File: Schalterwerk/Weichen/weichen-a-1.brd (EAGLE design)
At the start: 86 x 30.5 mm, 44 parts, among them J1 PHNX_2P_508CONN_1017491, Q1 P-MOSFET, Q2 P-MOSFET, Q3 P-MOSFET, Q4 P-MOSFET, X1 PHNX_4P_508CONN_1017493, X2 PHNX_4P_350CONN_1984989_PXC, X3 PHNX_4P_350CONN_1984989_PXC, X4 RJ45-JACK

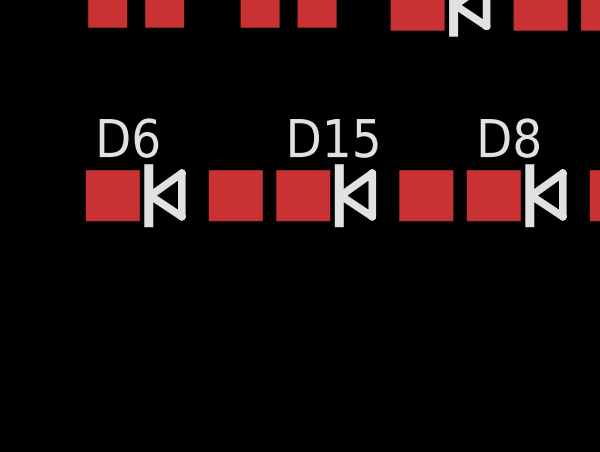
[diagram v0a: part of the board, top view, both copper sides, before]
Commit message: Closes out first release of Weichenschaltung.
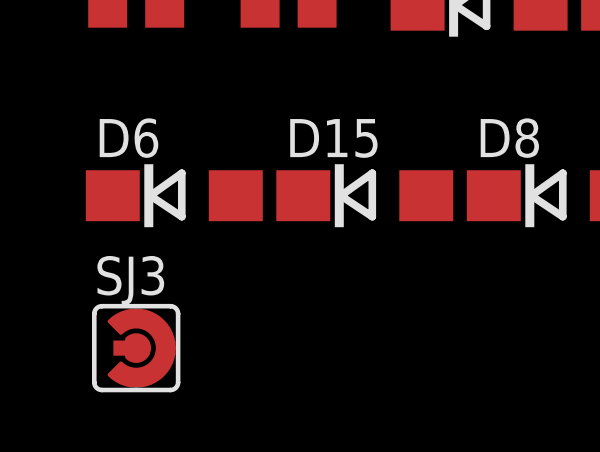
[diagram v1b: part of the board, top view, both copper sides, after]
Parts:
- added SJ3: (no value), eagleparts:SJ_RND2
- R1, R2, R3, R4: value 5k -> 10k
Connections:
- net GND: now also SJ3.P$1
- net L2: now also D10.C, D12.C, D3.A, D6.C, D8.C, R10.2, X1.5, X1.6; no longer D10.A, D11.A, D9.A, X1.3, X1.4
- net L3: now also D10.A, D11.A, D9.A, SJ3.P$2, X1.3, X1.4; no longer D10.C, D12.C, D3.A, D6.C, D8.C, R10.2, X1.5, X1.6
- net N$16: now also OK1.2, OK1.4; no longer OK1.6, OK1.8
- net N$24: now also OK1.1; no longer OK1.5
- net N$25: now also OK1.3; no longer OK1.7
- net N$27: now also OK1.16; no longer OK1.12
- net N$30: now also OK1.14; no longer OK1.10
- net N$35: now also OK1.15; no longer OK1.11
- net N$37: now also OK1.13; no longer OK1.9
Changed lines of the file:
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@@
 <attribute name="VALUE" x="4.35" y="-419.04" size="1.27" layer="27" align="top-left"/>
 </element>
-<element name="R1" library="rcl" library_urn="urn:adsk.eagle:library:334" package="R0805" package3d_urn="urn:adsk.eagle:package:23553/2" value="5k" x="2.54" y="-424.18" smashed="yes">
+<element name="R1" library="rcl" library_urn="urn:adsk.eagle:library:334" package="R0805" package3d_urn="urn:adsk.eagle:package:23553/2" value="10k" x="2.54" y="-424.18" smashed="yes">
 <attribute name="NAME" x="1.905" y="-422.91" size="1.27" layer="25"/>
 <attribute name="POPULARITY" value="86" x="2.54" y="-424.18" size="1.778" layer="27" display="off"/>
@@
 <attribute name="VALUE" x="4.35" y="-443.17" size="1.27" layer="27" align="top-left"/>
 </element>
-<element name="R2" library="rcl" library_urn="urn:adsk.eagle:library:334" package="R0805" package3d_urn="urn:adsk.eagle:package:23553/2" value="5k" x="2.54" y="-448.31" smashed="yes">
+<element name="R2" library="rcl" library_urn="urn:adsk.eagle:library:334" package="R0805" package3d_urn="urn:adsk.eagle:package:23553/2" value="10k" x="2.54" y="-448.31" smashed="yes">
 <attribute name="NAME" x="1.905" y="-447.04" size="1.27" layer="25"/>
 <attribute name="POPULARITY" value="86" x="2.54" y="-448.31" size="1.778" layer="27" display="off"/>
@@
 <attribute name="VALUE" x="4.35" y="-573.98" size="1.27" layer="27" align="top-left"/>
 </element>
-<element name="R3" library="rcl" library_urn="urn:adsk.eagle:library:334" package="R0805" package3d_urn="urn:adsk.eagle:package:23553/2" value="5k" x="7.62" y="-590.55" smashed="yes">
+<element name="R3" library="rcl" library_urn="urn:adsk.eagle:library:334" package="R0805" package3d_urn="urn:adsk.eagle:package:23553/2" value="10k" x="7.62" y="-590.55" smashed="yes">
 <attribute name="NAME" x="6.985" y="-589.28" size="1.27" layer="25"/>
 <attribute name="POPULARITY" value="86" x="2.54" y="-579.12" size="1.778" layer="27" display="off"/>
@@
 <attribute name="VALUE" x="4.35" y="-585.41" size="1.27" layer="27" align="top-left"/>
 </element>
-<element name="R4" library="rcl" library_urn="urn:adsk.eagle:library:334" package="R0805" package3d_urn="urn:adsk.eagle:package:23553/2" value="5k" x="2.54" y="-590.55" smashed="yes">
+<element name="R4" library="rcl" library_urn="urn:adsk.eagle:library:334" package="R0805" package3d_urn="urn:adsk.eagle:package:23553/2" value="10k" x="2.54" y="-590.55" smashed="yes">
 <attribute name="NAME" x="1.905" y="-589.28" size="1.27" layer="25"/>
 <attribute name="POPULARITY" value="86" x="2.54" y="-603.25" size="1.778" layer="27" display="off"/>
@@
 <attribute name="POPULARITY" value="14" x="3.81" y="-641.35" size="1.778" layer="27" display="off"/>
 <attribute name="VALUE" x="20.22" y="-599.456" size="1.27" layer="27" ratio="10"/>
+</element>
+<element name="SJ3" library="eagleparts" package="SJ_RND2" value="" x="2.54" y="-601.98" smashed="yes">
+<attribute name="NAME" x="1.143" y="-600.202" size="1.27" layer="25" ratio="10"/>
 </element>
 </elements>
@@
 <contactref element="X4" pad="8"/>
 <contactref element="X3" pad="4"/>
-<contactref element="OK1" pad="6"/>
-<contactref element="OK1" pad="8"/>
+<contactref element="OK1" pad="2"/>
+<contactref element="OK1" pad="4"/>
 <wire x1="30.82" y1="-158.75" x2="6.605" y2="-187.45" width="0" layer="19" extent="1-1"/>
-<wire x1="16.51" y1="-554.99" x2="6.605" y2="-187.45" width="0" layer="19" extent="1-1"/>
-<wire x1="21.59" y1="-554.99" x2="16.51" y2="-554.99" width="0" layer="19" extent="1-1"/>
+<wire x1="6.35" y1="-554.99" x2="6.605" y2="-187.45" width="0" layer="19" extent="1-1"/>
+<wire x1="11.43" y1="-554.99" x2="6.35" y2="-554.99" width="0" layer="19" extent="1-1"/>
 </signal>
 <signal name="N$20">
@@
 <wire x1="1.59" y1="-541.02" x2="3.556" y2="-364.49" width="0" layer="19" extent="1-1"/>
 </signal>
-<signal name="L3">
+<signal name="L2">
 <contactref element="D6" pad="C"/>
 <contactref element="D8" pad="C"/>
@@
 <contactref element="J1" pad="3"/>
 <contactref element="J1" pad="4"/>
+<contactref element="SJ3" pad="P$1"/>
 <wire x1="26.67" y1="-472.63" x2="26.67" y2="-481.33" width="0" layer="19" extent="1-1"/>
+<wire x1="2.286" y1="-601.98" x2="26.67" y2="-481.33" width="0" layer="19" extent="1-1"/>
 </signal>
 <signal name="+12V">
@@
 <wire x1="21.59" y1="-15.43" x2="21.59" y2="-24.13" width="0" layer="19" extent="1-1"/>
 </signal>
-<signal name="L2">
+<signal name="L3">
 <contactref element="X1" pad="4"/>
 <contactref element="X1" pad="3"/>
@@
 <contactref element="D9" pad="A"/>
 <contactref element="D10" pad="A"/>
+<contactref element="SJ3" pad="P$2"/>
 <wire x1="5.86" y1="-402.59" x2="5.86" y2="-407.67" width="0" layer="19" extent="1-1"/>
 <wire x1="5.86" y1="-397.51" x2="5.86" y2="-402.59" width="0" layer="19" extent="1-1"/>
+<wire x1="3.556" y1="-601.98" x2="5.86" y2="-407.67" width="0" layer="19" extent="1-1"/>
 <wire x1="26.67" y1="-24.13" x2="5.86" y2="-397.51" width="0" layer="19" extent="1-1"/>
 <wire x1="26.67" y1="-15.43" x2="26.67" y2="-24.13" width="0" layer="19" extent="1-1"/>
@@
 <signal name="N$24">
 <contactref element="R15" pad="2"/>
-<contactref element="OK1" pad="5"/>
-<wire x1="13.97" y1="-554.99" x2="3.49" y2="-346.71" width="0" layer="19" extent="1-1"/>
+<contactref element="OK1" pad="1"/>
+<wire x1="3.81" y1="-554.99" x2="3.49" y2="-346.71" width="0" layer="19" extent="1-1"/>
 </signal>
 <signal name="N$25">
-<contactref element="OK1" pad="7"/>
 <contactref element="R16" pad="2"/>
-<wire x1="19.05" y1="-554.99" x2="3.49" y2="-561.34" width="0" layer="19" extent="1-1"/>
+<contactref element="OK1" pad="3"/>
+<wire x1="8.89" y1="-554.99" x2="3.49" y2="-561.34" width="0" layer="19" extent="1-1"/>
 </signal>
 <signal name="N$29">
@@
 <signal name="N$35">
 <contactref element="D14" pad="A"/>
-<contactref element="OK1" pad="11"/>
-<wire x1="16.51" y1="-547.37" x2="22.37" y2="-590.55" width="0" layer="19" extent="1-1"/>
+<contactref element="OK1" pad="15"/>
+<wire x1="6.35" y1="-547.37" x2="22.37" y2="-590.55" width="0" layer="19" extent="1-1"/>
 </signal>
 <signal name="N$36">
@@
 <signal name="N$37">
 <contactref element="D15" pad="A"/>
-<contactref element="OK1" pad="9"/>
-<wire x1="21.59" y1="-547.37" x2="12.21" y2="-596.9" width="0" layer="19" extent="1-1"/>
+<contactref element="OK1" pad="13"/>
+<wire x1="11.43" y1="-547.37" x2="12.21" y2="-596.9" width="0" layer="19" extent="1-1"/>
 </signal>
 <signal name="N$38">
@@
 </signal>
 <signal name="N$27">
-<contactref element="OK1" pad="12"/>
 <contactref element="R7" pad="2"/>
-<wire x1="13.97" y1="-547.37" x2="17.46" y2="-579.12" width="0" layer="19" extent="1-1"/>
+<contactref element="OK1" pad="16"/>
+<wire x1="3.81" y1="-547.37" x2="17.46" y2="-579.12" width="0" layer="19" extent="1-1"/>
 </signal>
 <signal name="N$30">
 <contactref element="R8" pad="2"/>
-<contactref element="OK1" pad="10"/>
-<wire x1="19.05" y1="-547.37" x2="23.81" y2="-579.12" width="0" layer="19" extent="1-1"/>
+<contactref element="OK1" pad="14"/>
+<wire x1="8.89" y1="-547.37" x2="23.81" y2="-579.12" width="0" layer="19" extent="1-1"/>
 </signal>
 </signals>
